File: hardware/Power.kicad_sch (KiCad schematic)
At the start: 70 parts, among them J10 I2C, J3 ESTOP, J4 PWR, J5 Conn_ARM_JTAG_SWD_10, J7 FAN, J9 DEBUG, Q1 MMBT5401LT1G, Q2 PSMN4R8-100BSEJ, Q3 MMBT3904, Q5 PSMN4R8-100BSEJ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

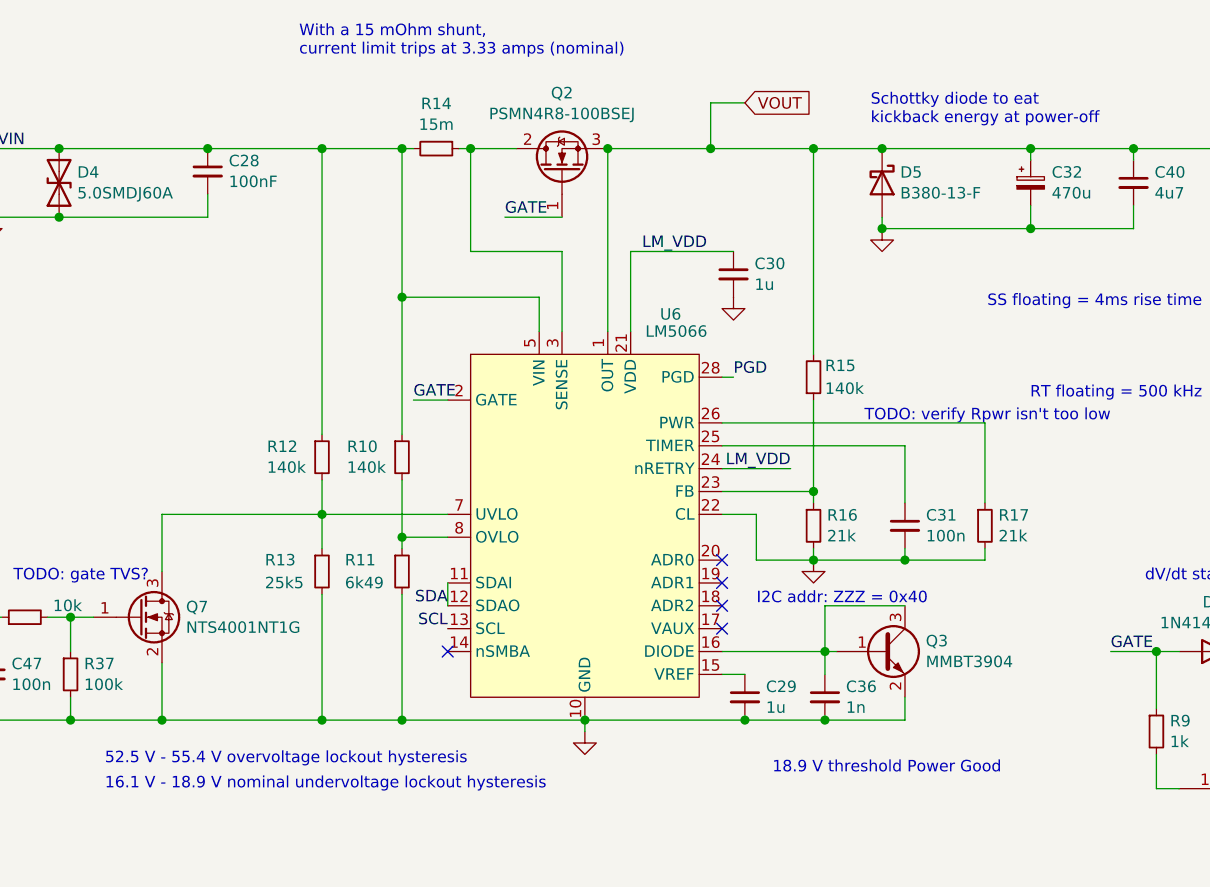
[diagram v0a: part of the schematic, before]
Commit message: Power Bump to 530W+ (#3)
* Rsns to 5m (13A limit)

* Adding resistors for external divider (allows higher current sense)

* Adjusting timeout capacitor (1uF -> 52ms)

* Adjusting feedback resistors.

* Adding ERD resistors to layout.

* Revert "Adjusting timeout capacitor (1uF -> 52ms)"

This reverts commit 7a30909a9925d87866bd3a766fa9658db1f002d2.

* Removing external resistor divider.

* Bumping Rpwr

* Adjusting Timer (C31)

* Updating info from schematic

* Adding second Power FET

* Revert "Adding second Power FET"

This reverts commit e632f1e0367ea6556d8bc6e08f99c25e5b9f6e16.
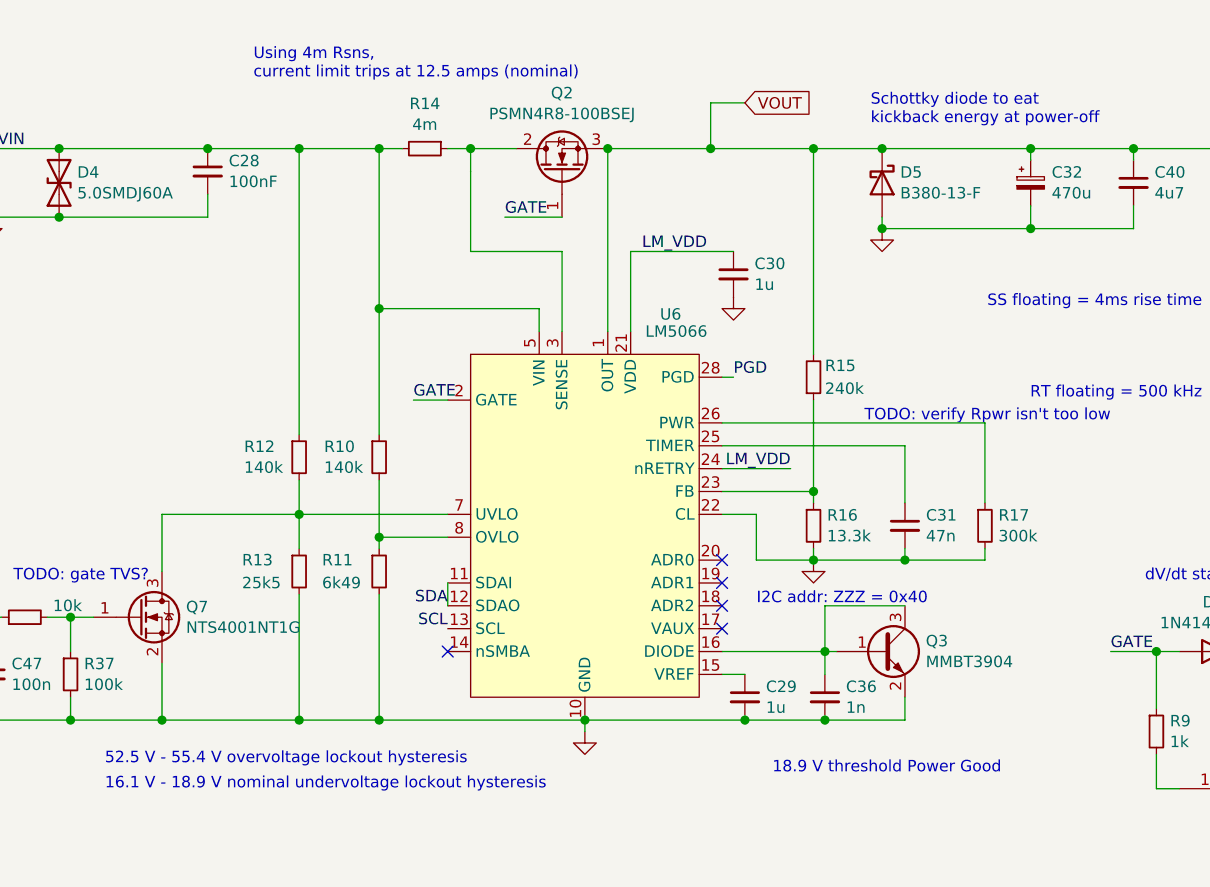
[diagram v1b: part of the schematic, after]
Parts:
- C31: value 100n -> 47n; D1PN 311-1344-1-ND -> 1276-2070-2-ND; MFN Yageo -> Samsung Electro-Mechanics; MPN CC0603KRX7R9BB104 -> CL10B473JB8NNNC
- R14: value 15m -> 4m; D1PN WSLH-.015CT-ND -> WSLH-.004TR-ND; MPN WSL2512R0150FEA18 -> WSL25124L000FEA18
- R15: value 140k -> 240k; D1PN P140KDBCT-ND -> P240KDBTR-ND; MPN ERA-3AEB1403V -> ERA-3AEB244V
- R16: value 21k -> 13.3k; D1PN P21KDBCT-ND -> P13.3KDBTR-ND; MPN ERA-3AEB2102V -> ERA-3AEB1332V
- R17: value 21k -> 300k; D1PN P21KDBCT-ND -> P300KDBTR-ND; MPN ERA-3AEB2102V -> ERA-3AEB304V
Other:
- note added: "Using 4m Rsns, current limit trips at 12.5 amps (nominal)"
- note removed: "With a 15 mOhm shunt, current limit trips at 3.33 amps (nominal)"
- moved on the sheet: R10, R11, R12, R13, R14

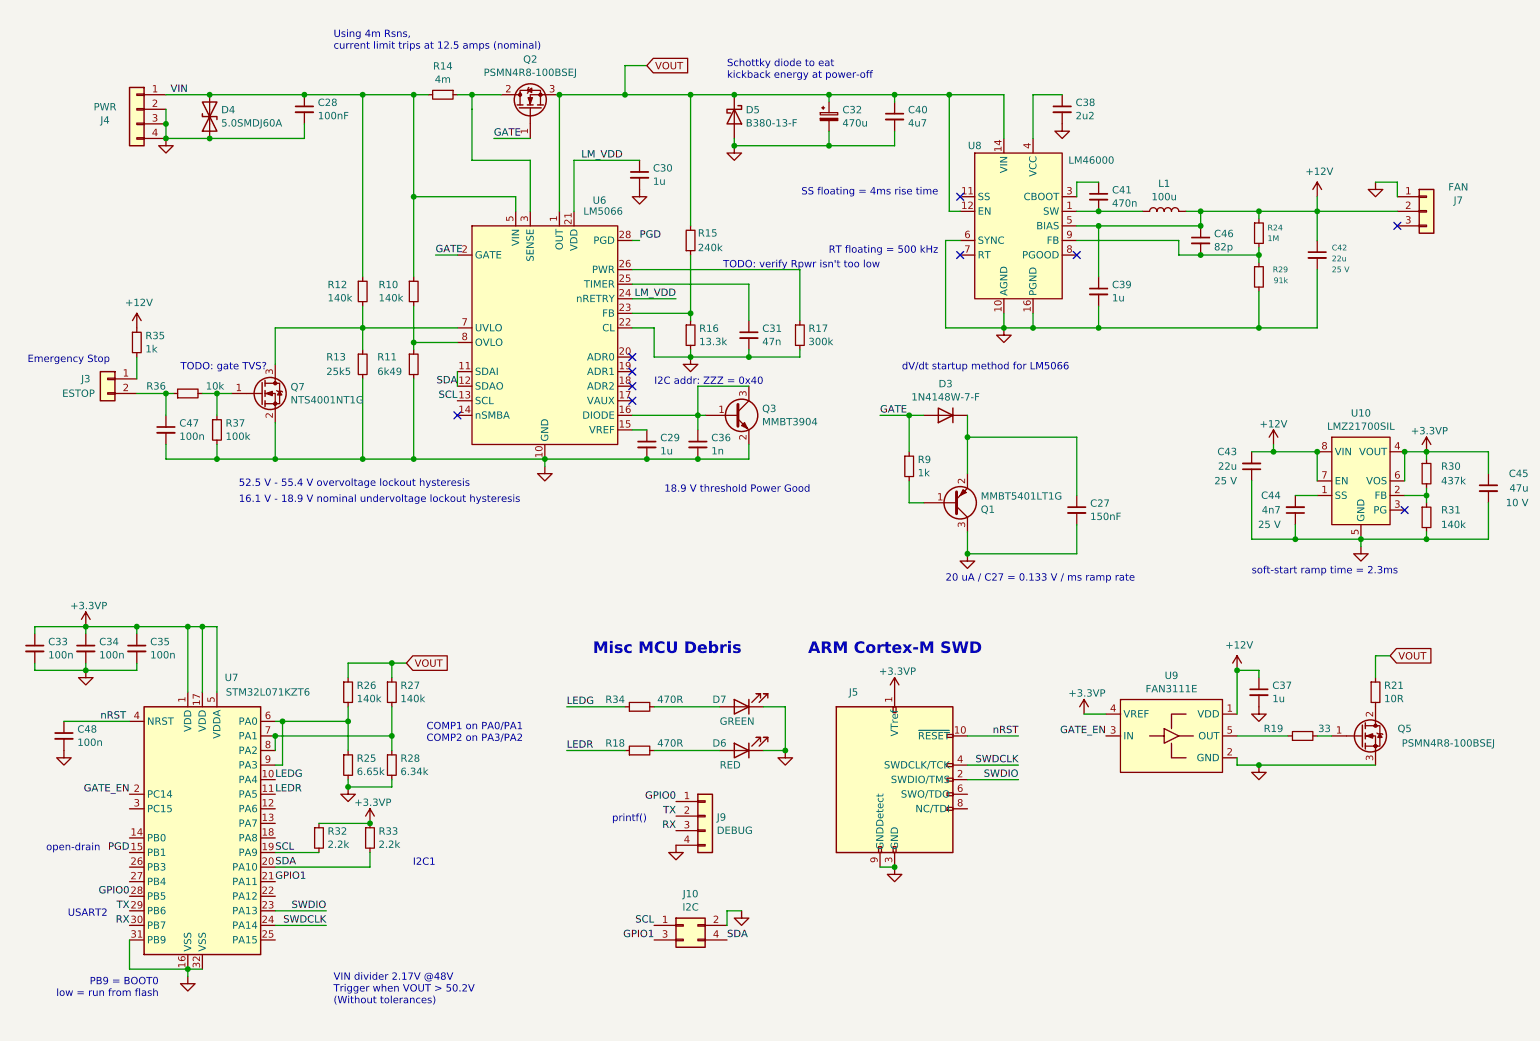
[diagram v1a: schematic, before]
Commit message: Adding second Power FET
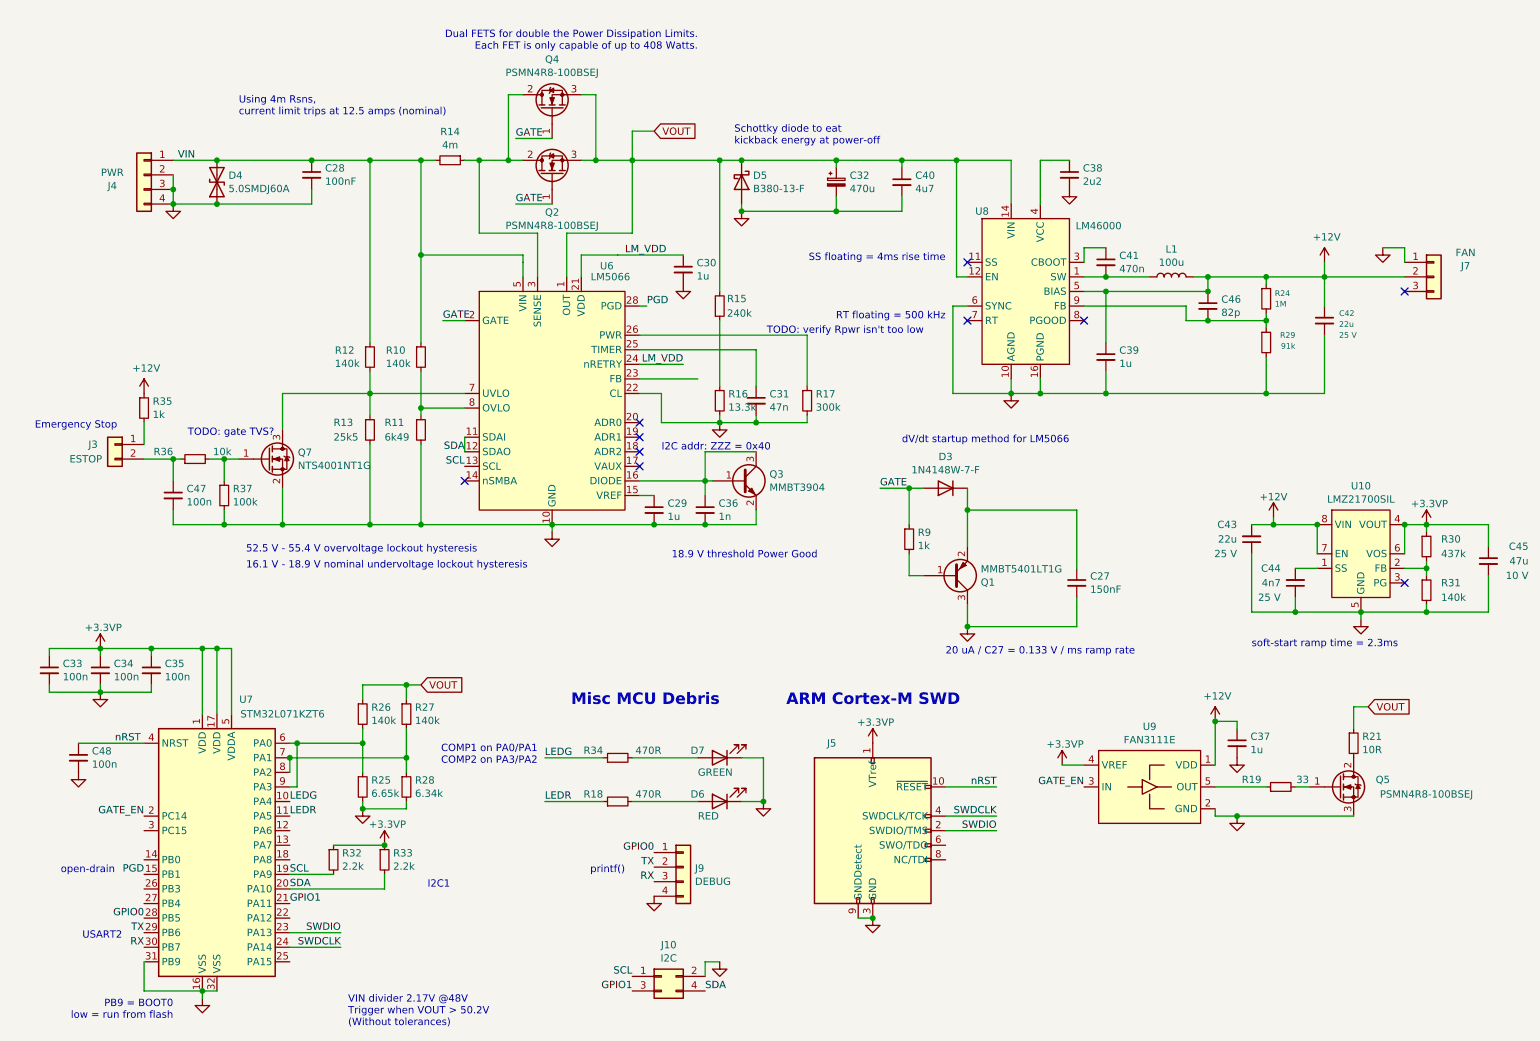
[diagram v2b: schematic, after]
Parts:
- added Q4: PSMN4R8-100BSEJ, Package_TO_SOT_SMD:TO-263-2, symbol Device:Q_NMOS_GDS
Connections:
- net GATE: now also Q4.1 (G)
- net VOUT: now also Q4.3 (S)
- net at Q2.2 (D), R14.1, U6.3 (SENSE): now also Q4.2 (D)
- net at R15.1, R16.1: no longer U6.23 (FB)
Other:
- note added: "Dual FETS for double the Power Dissipation Limits. Each FET is only capable of up to 408 Watts."
- moved on the sheet: C27, C28, C29, C30, C31, C32, C33, C34, C35, C36, C37, C38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

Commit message: Revert "Adding second Power FET"
This reverts commit e632f1e0367ea6556d8bc6e08f99c25e5b9f6e16.
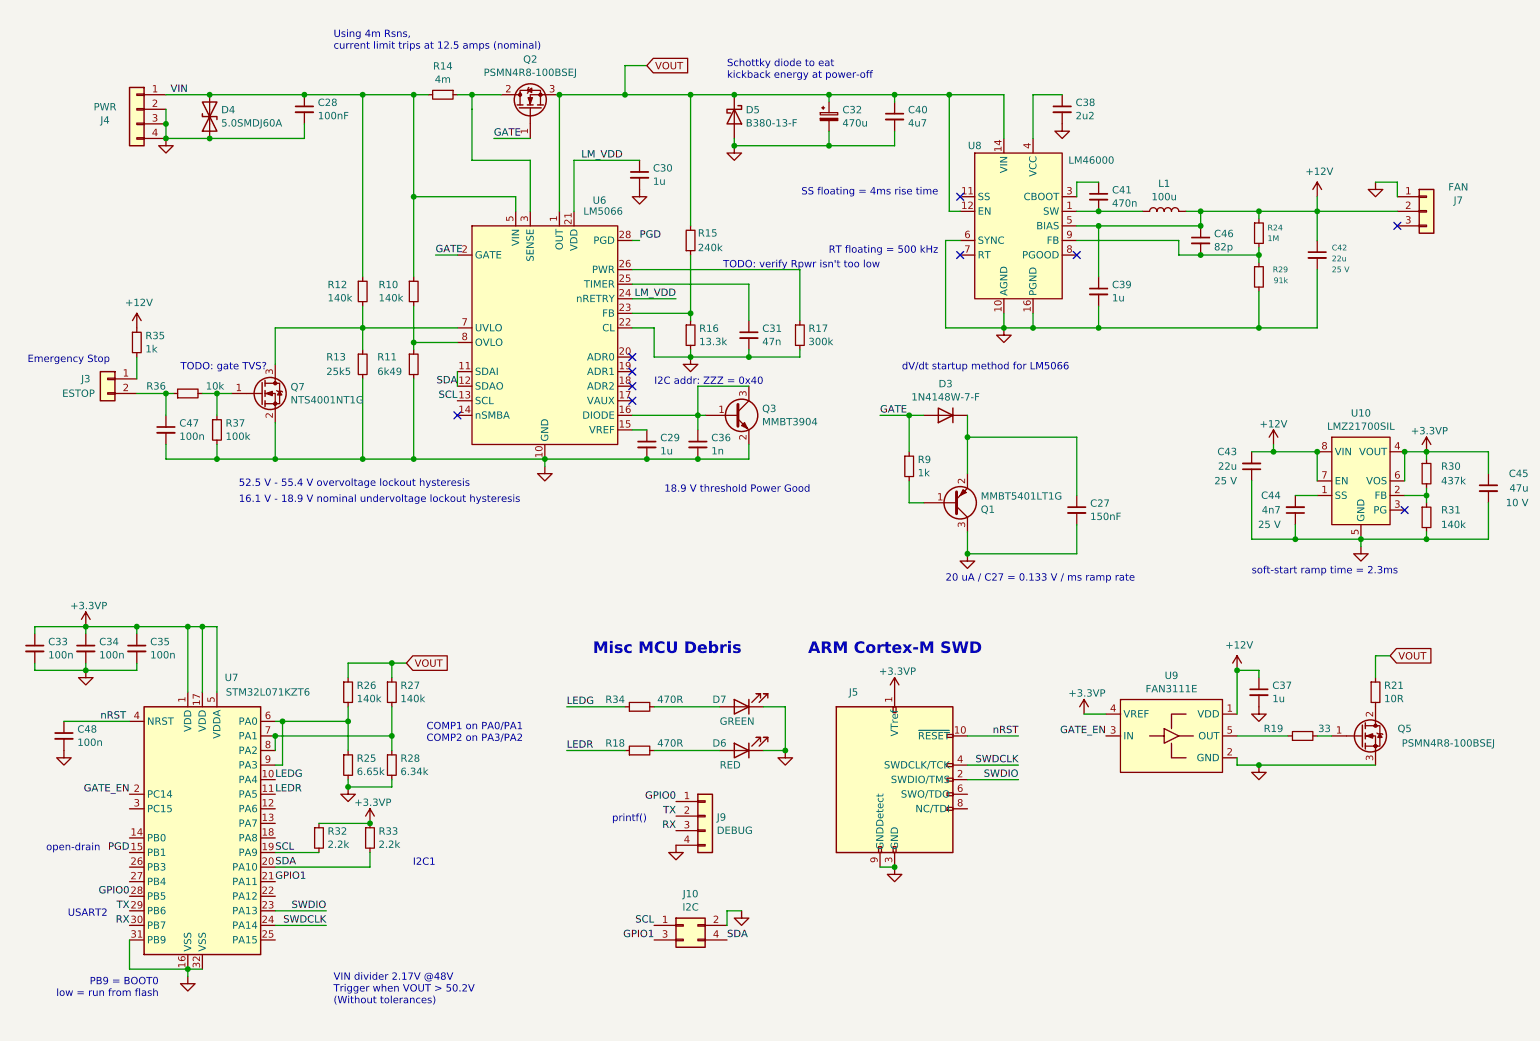
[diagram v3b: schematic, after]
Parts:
- removed Q4: PSMN4R8-100BSEJ, Package_TO_SOT_SMD:TO-263-2, symbol Device:Q_NMOS_GDS
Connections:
- net at R15.1, R16.1: now also U6.23 (FB)
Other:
- note removed: "Dual FETS for double the Power Dissipation Limits. Each FET is only capable of up to 408 Watts."
- moved on the sheet: C27, C28, C29, C30, C31, C32, C33, C34, C35, C36, C37, C38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
